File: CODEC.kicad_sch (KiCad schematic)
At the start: 9 parts, among them U4 NAU8810YG, U5 MAX98307ETE+T, U6 AD8532ARZ-REEL7

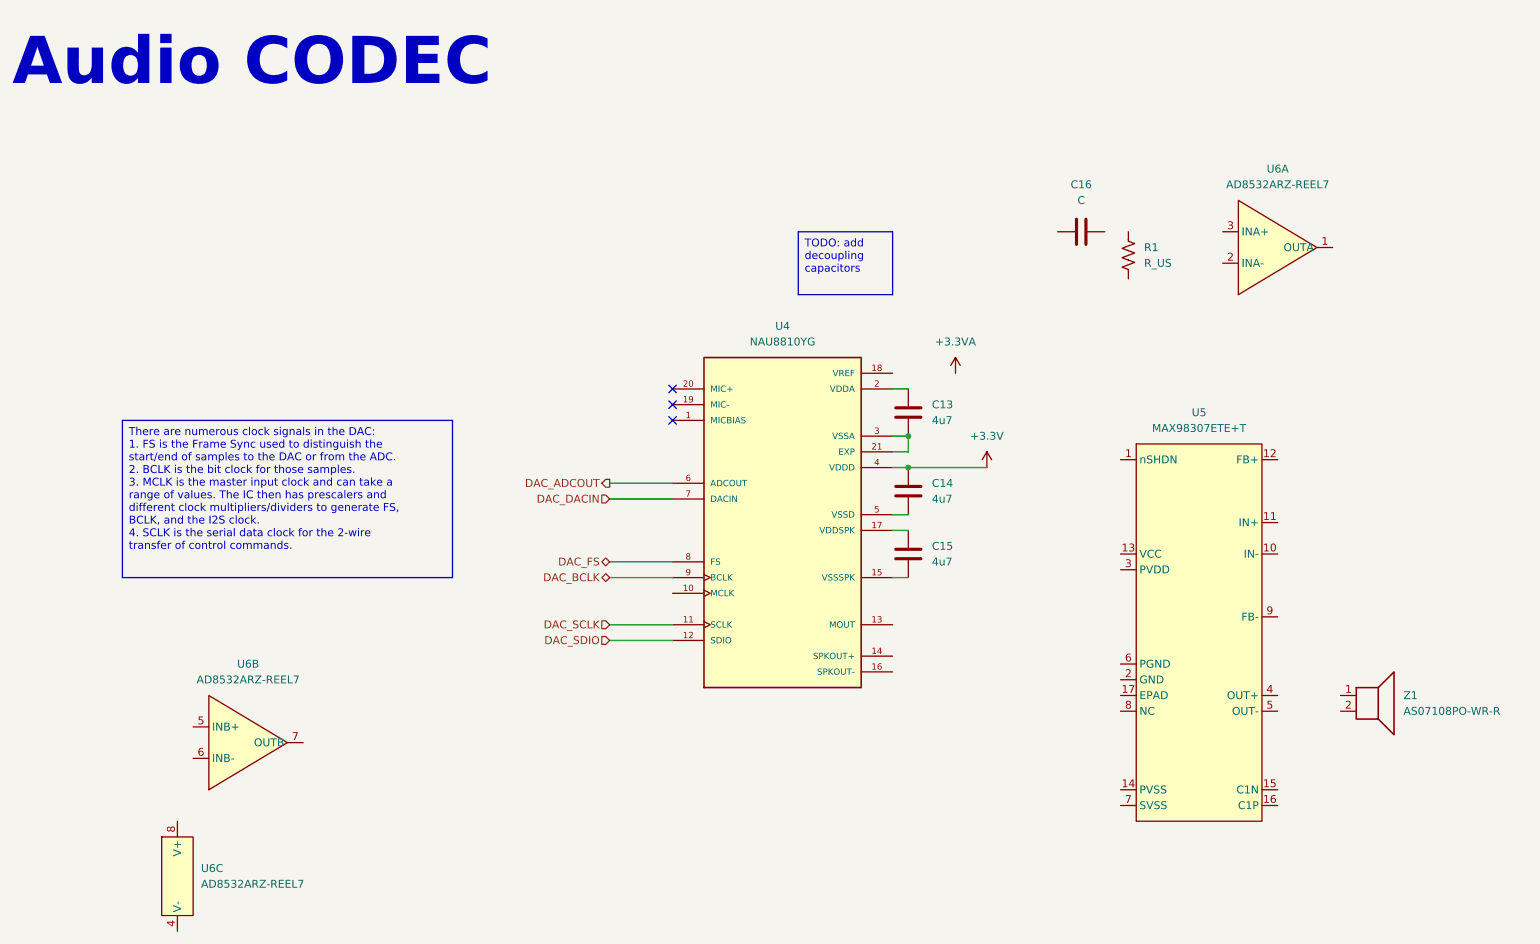
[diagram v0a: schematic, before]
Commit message: Worked more on CODEC sheet, beginning symbol for new MCU part chosen
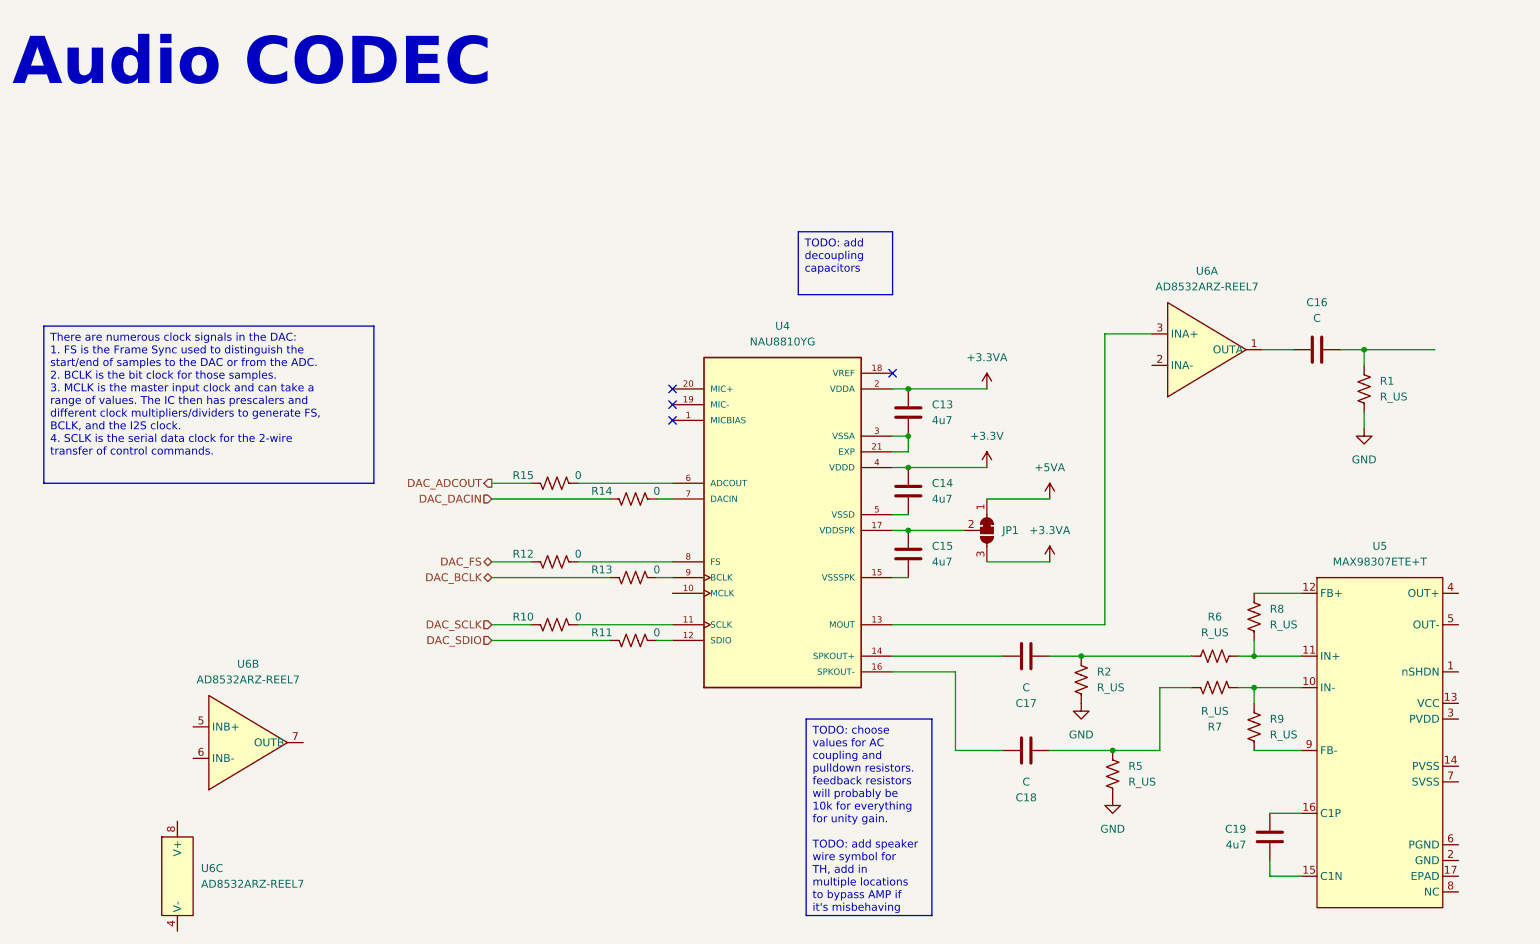
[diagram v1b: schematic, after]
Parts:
- removed Z1: AS07108PO-WR-R, symbol Device:Speaker
- added C17, C18: C, symbol Device:C
- added C19: 4u7, symbol Device:C
- added JP1: SolderJumper_3_Bridged12, symbol Jumper:SolderJumper_3_Bridged12
- added R10, R11, R12, R13, R14, R15: 0, symbol Device:R_US
- added R2, R5, R6, R7, R8, R9: R_US, symbol Device:R_US
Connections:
- net +3.3VA: now also C13.1, U4.2 (VDDA), JP1.3 (B)
- net DAC_ADCOUT: now also R15.1; no longer U4.6 (ADCOUT)
- net DAC_BCLK: now also R13.1; no longer U4.9 (BCLK)
- net DAC_DACIN: now also R14.1; no longer U4.7 (DACIN)
- net DAC_FS: now also R12.1; no longer U4.8 (FS)
- net DAC_SCLK: now also R10.1; no longer U4.11 (SCLK)
- net DAC_SDIO: now also R11.1; no longer U4.12 (SDIO)
- net at U5.10 (IN-): now also R7.2, R9.2
- net at U5.11 (IN+): now also R6.2, R8.1
- net at U5.12 (FB+): now also R8.2
- net at U5.15 (C1N): now also C19.2
- net at U5.16 (C1P): now also C19.1
- net at U5.9 (FB-): now also R9.1
- net at C15.1, U4.17 (VDDSPK): now also JP1.2 (C)
- net at R1.1: now also C16.1
- net GND: now reaches R1.2
- net GND: now also R2.2, R5.2
- net at U6.1 (OUTA): now also C16.2
- net at U6.3 (INA+): now also U4.13 (MOUT)
- net at U4.14 (SPKOUT+): now also C17.1
- net at U4.16 (SPKOUT-): now also C18.1
- new net: C17.2, R2.1, R6.1
- new net: R12.2, U4.8 (FS)
- new net: C18.2, R5.1, R7.1
- new net: R11.2, U4.12 (SDIO)
- new net: R10.2, U4.11 (SCLK)
- new net: R13.2, U4.9 (BCLK)
- new net: R15.2, U4.6 (ADCOUT)
- new net: R14.2, U4.7 (DACIN)
- new net +5VA: JP1.1 (A)
- no-connect marks 3 -> 4
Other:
- moved on the sheet: C16, R1, U5, U6A
